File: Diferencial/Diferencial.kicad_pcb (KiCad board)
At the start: 2 copper layers, 100 x 100 mm, 112 parts, among them J1 Pedal Sensor 1, J2 Pedal Sensor 2, J3 Brake Sensor 1, J4 Brake Sensor 2, J5 Out_Brake_Light, J6 Buzzer_out, J7 Screw_Terminal_01x04, J8 DB9_Female, K1 RELAY_19.1x15.5mm, Q1 MMBT3904, Q2 MMBT3904, U1 LM358, U2 UFRGS_PILL, U3 LM358, U4 MCP2558FD-xSN, U5 LM317_3PinPackage

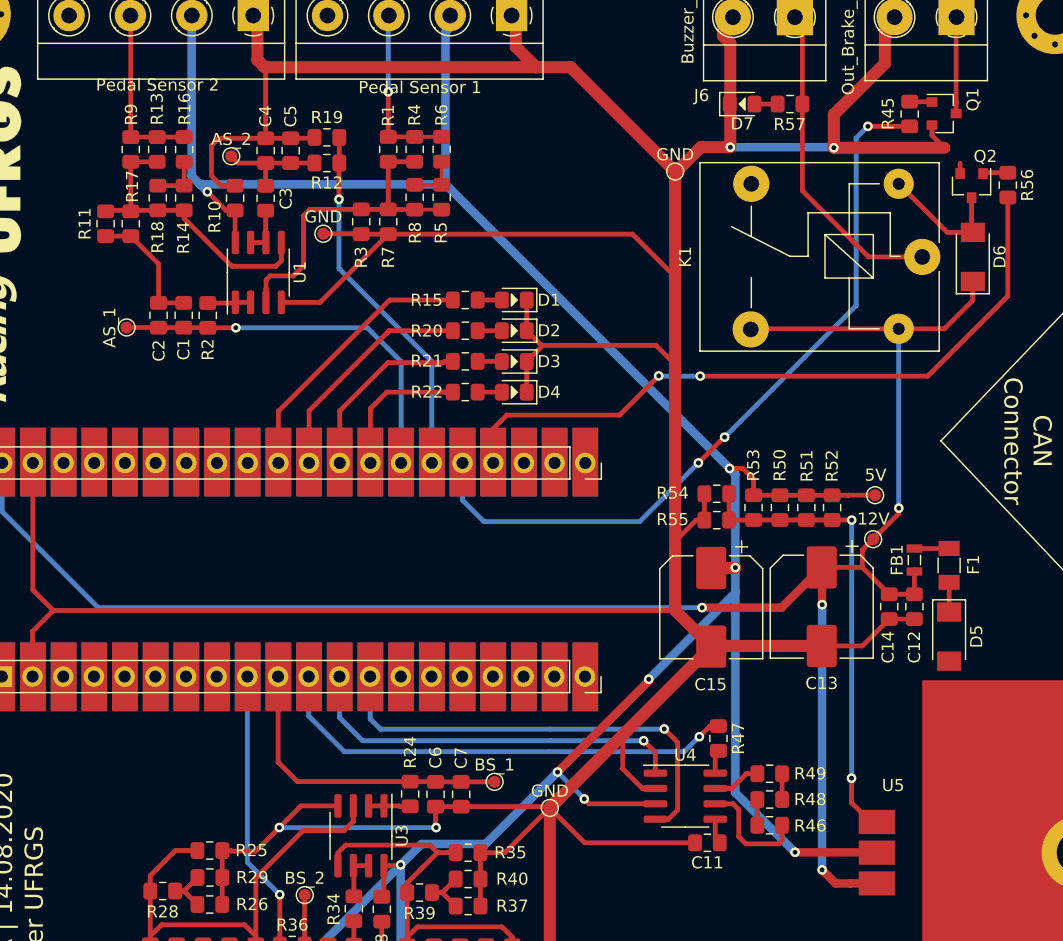
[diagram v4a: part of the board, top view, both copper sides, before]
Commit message: Layout Fixes and CAN Connector Added
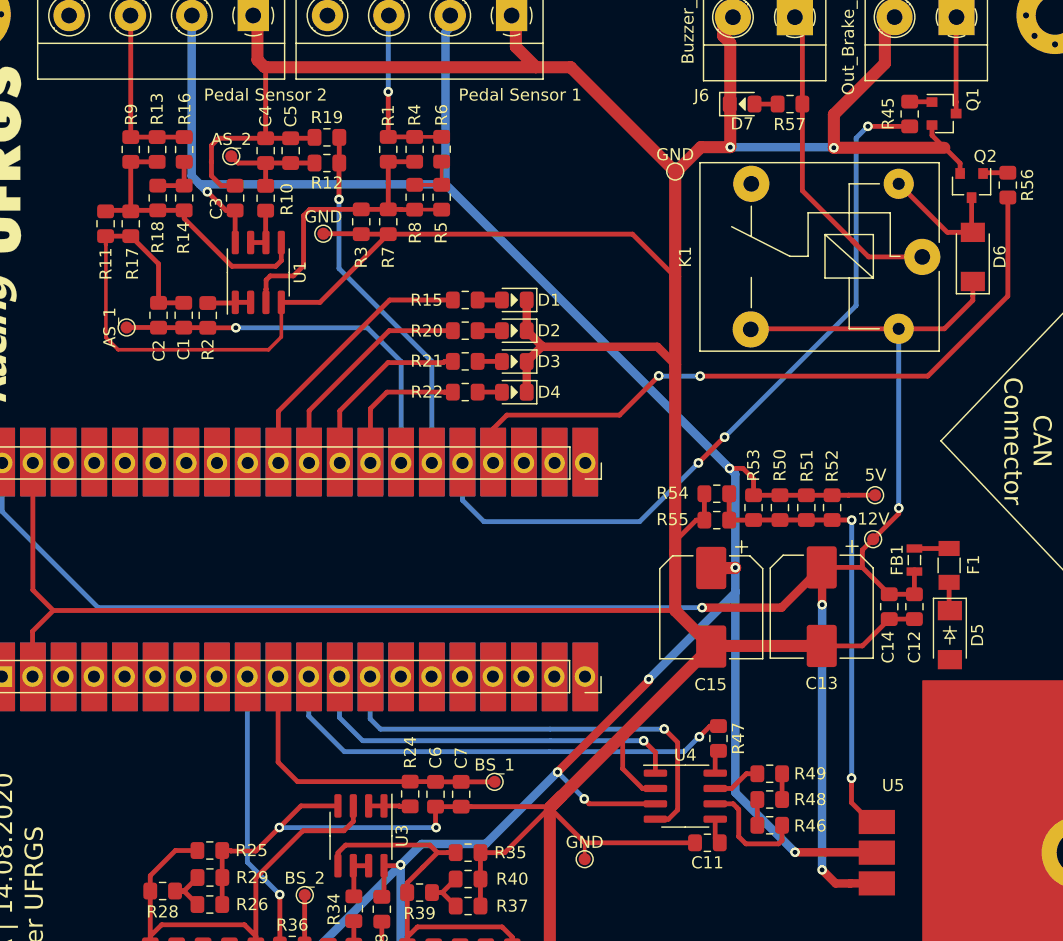
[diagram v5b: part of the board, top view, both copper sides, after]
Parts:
- D5: value D_SCH_SS54HF -> SS54HF
- moved TP5 5.13 mm to (120.9, 143.3)
- moved D5 0.14 mm to (151.1, 124.7)
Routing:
- net GND: track 596.0 -> 637.5 mm

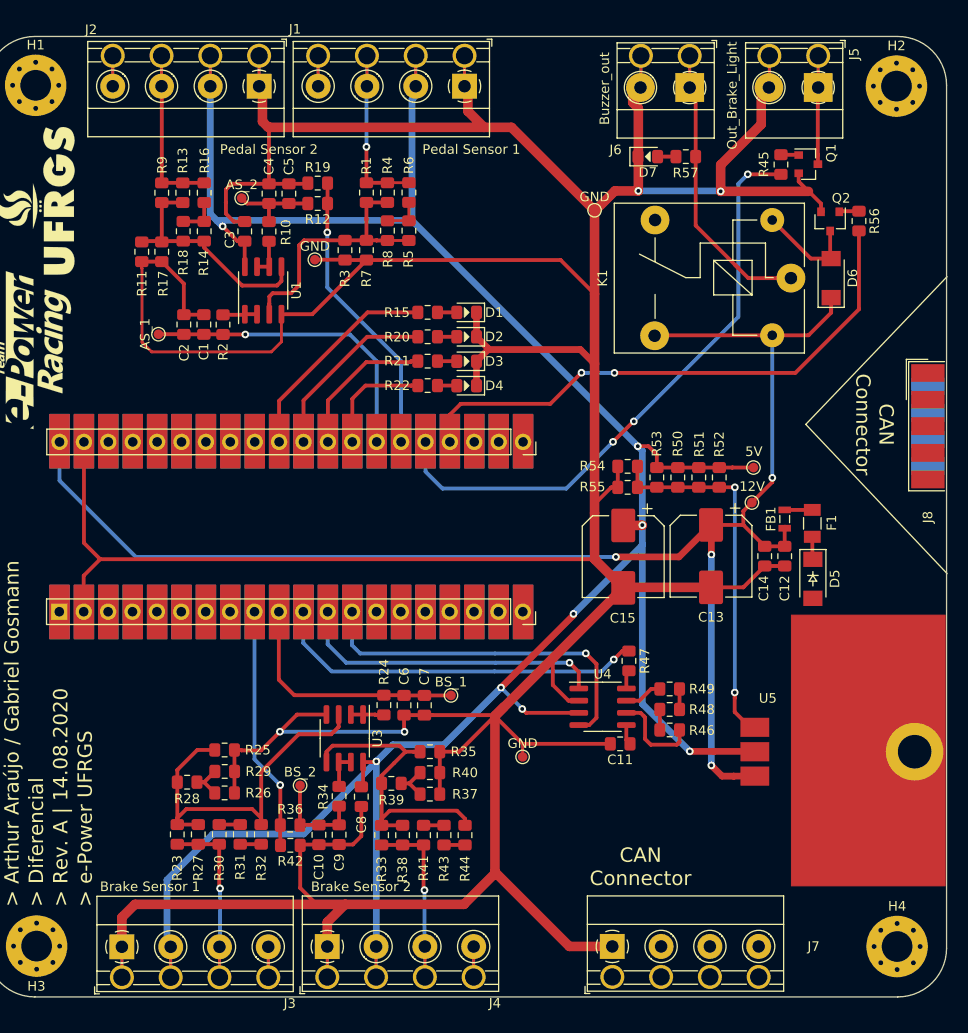
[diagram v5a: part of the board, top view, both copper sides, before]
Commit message: Added CAN connectors / Fixes
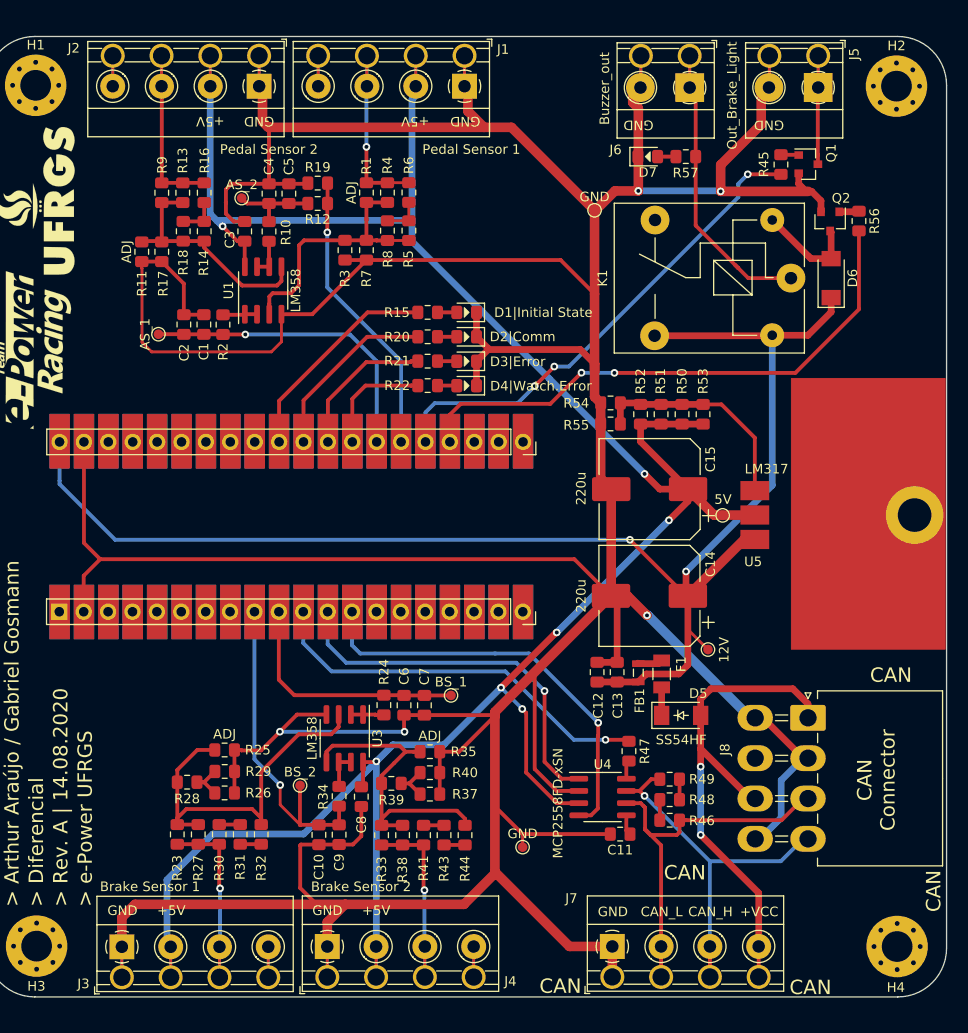
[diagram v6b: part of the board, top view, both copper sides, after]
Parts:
- removed R36, R42: 10K, Resistor_SMD:R_0805_2012Metric_Pad1.15x1.40mm_HandSolder
- removed TP8: GND, e-Power:TestPoint_Pad_D1.0mm
- C14, C15: footprint Capacitor_SMD:CP_Elec_8x10 -> Capacitor_SMD:CP_Elec_10x10
- D1|Initial State: renamed from D1
- J8: value DB9_Female -> CAN_1; footprint e-Power:DSUB-9_Female_EdgeMount_P2.77mm -> e-Power:Molex_Mini-Fit_Jr_2x04_P4.20mm_Horizontal
- U5: value LM317_3PinPackage -> LM317
- moved J8 32.8 mm to (150.6, 139.2), turned to 270 degrees
- moved U5 24.6 mm to (145.1, 115.5)
- moved C12 23.0 mm to (128.7, 134.4), turned to 90 degrees
- moved F1 22.2 mm to (135.4, 134.6)
- moved FB1 22.1 mm to (133.0, 134.5)
- moved D5 19.8 mm to (137.4, 138.9), turned to 0 degrees
- moved C13 19.5 mm to (130.7, 134.4), turned to 90 degrees
- moved TP1 16.0 mm to (140.2, 132.1), turned to 0 degrees
- moved R52 10.5 mm to (133.2, 107.6), turned to 90 degrees
- moved C11 9.40 mm to (131.1, 151.3)
- moved R46 9.40 mm to (136.2, 149.8)
- moved R47 9.40 mm to (132.0, 142.7)
- moved R48 9.40 mm to (136.2, 147.7)
- moved R49 9.40 mm to (136.2, 145.6)
- moved TP5 9.40 mm to (120.9, 152.7)
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- renumbered D2 to D2|Comm, D3 to D3|Error, D4 to D4|Watch.Error
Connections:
- C10 pad 2: Net-(C10-Pad2) -> /Brake_Sensor_2
- C9 pad 2: Net-(C10-Pad2) -> /Brake_Sensor_2
- J8 pad 2: /CAN_L -> GND
- J8 pad 3: GND -> /CAN_L
- J8 pad 4: (no net) -> /CAN_H
- J8 pad 6: GND -> (no net)
- J8 pad 7: /CAN_H -> /Input_Power
- J8 pad 8: (no net) -> GND
- R34 pad 2: Net-(C10-Pad2) -> /Brake_Sensor_2
- TP7 pad 1: Net-(C10-Pad2) -> /Brake_Sensor_2
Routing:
- net /Input_Power: track 0.00 -> 53.0 mm, vias 0 -> 2
- net GND: track 637.5 -> 672.2 mm, vias 4 -> 5
- net /CAN_H: track 4.35 -> 37.9 mm, vias 0 -> 1
- net /CAN_L: track 9.60 -> 40.0 mm
- net /Brake_Light: track 62.5 -> 51.2 mm
- net Net-(C10-Pad2): track 10.2 -> 0.00 mm
- net +5V: track 302.6 -> 293.0 mm, vias 8 -> 7
- net /Brake_Sensor_2: track 25.4 -> 34.3 mm
- net Net-(R50-Pad2): track 38.5 -> 29.7 mm, vias 2 -> 0
- net /TX: track 32.4 -> 39.7 mm
- net /RX: track 37.5 -> 43.7 mm
- net /S: track 39.3 -> 41.4 mm
- net Net-(D6-Pad2): track 10.6 -> 12.8 mm
- net +12V: track 159.9 -> 161.0 mm, vias 4 -> 2
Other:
- board text added: "+5V"
- board text added: "+VCC"
- board text added: "CAN"
- board text added: "CAN_H"
- board text added: "CAN_L"
- board text added: "GND"
